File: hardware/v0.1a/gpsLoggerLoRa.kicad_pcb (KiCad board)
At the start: 4 copper layers, 40.9 x 72.7 mm, 108 parts, among them J1 USB_C_Receptacle, J3 DF12 - 10P, J4 CTX TAG Connect, P2 CONN_01X02, Q1 FG6943010R, SW1 SW_Push, U1 SKY13373, U2 MCP73832, U3 NCP167, U4 SKY13373, U5 MT25QL256ABA8E12, U6 NCP167, U8 ATSAMR34J18B, Y1 32.768kHz

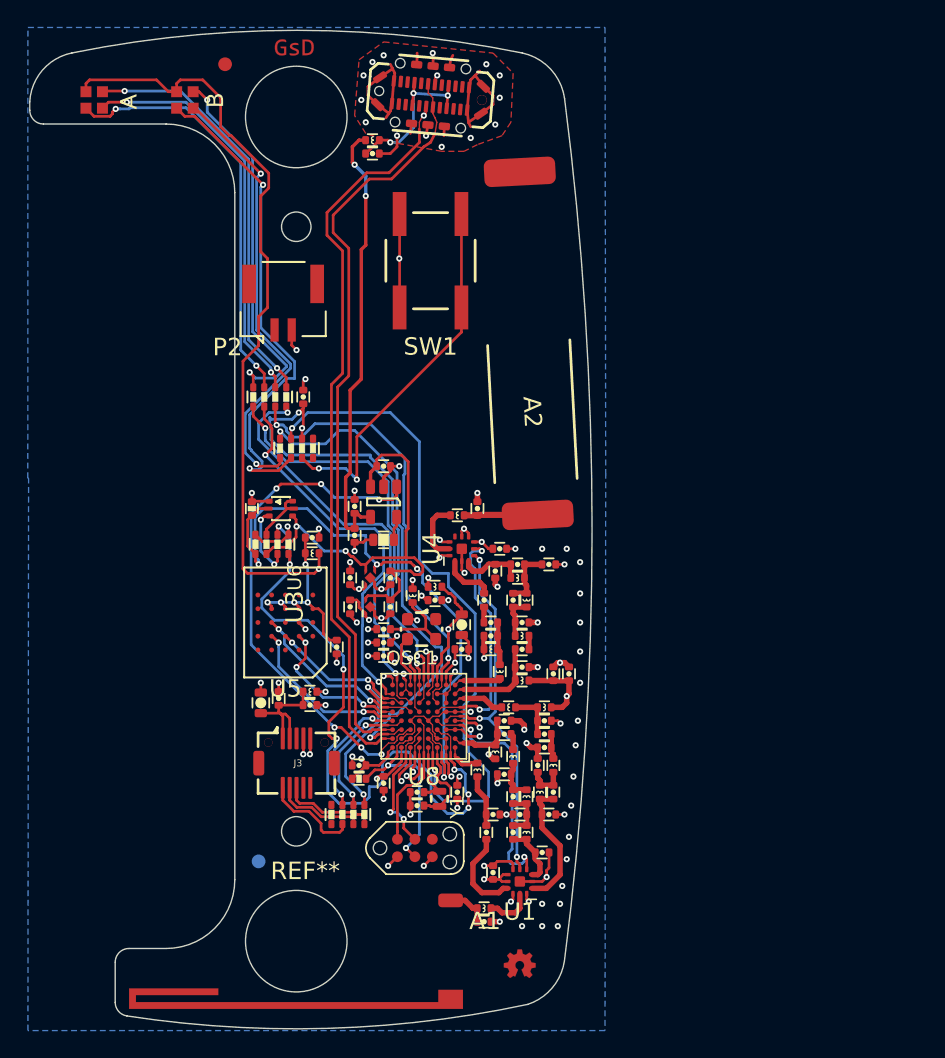
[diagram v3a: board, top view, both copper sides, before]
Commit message: Re-assigned IO pins. Added some extra filter as per Hardware guidelines.
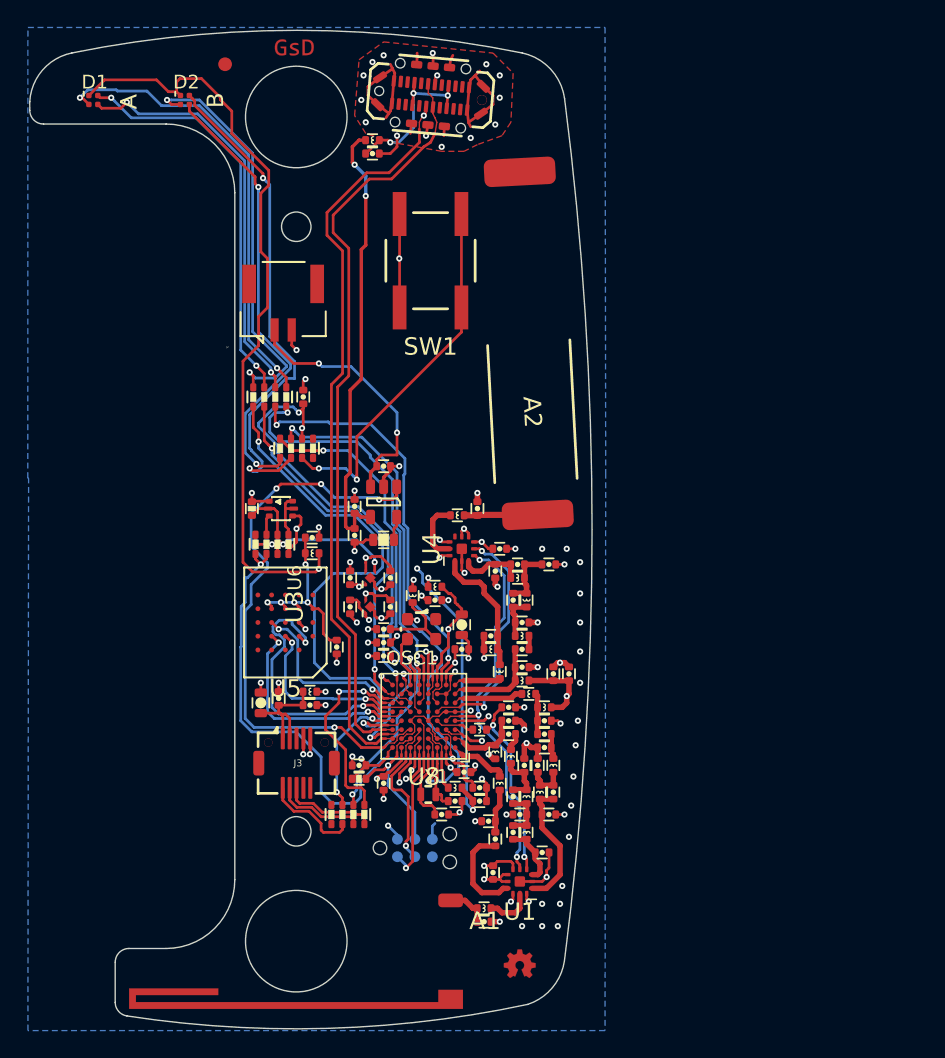
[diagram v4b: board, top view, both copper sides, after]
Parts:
- removed the REF** at (148.7, 126.7)
- added C57: 4.7pF, pkl_dipol:C_0402, F.Cu at (164.8, 121.3)
- added L23: 10nH, pkl_dipol:L_0402, F.Cu at (164.8, 117.1)
- added L24: 10nH, pkl_dipol:L_0402, F.Cu at (163.0, 121.3)
- C22, C27: value 18pF -> 4.7pF
- D1, D2: footprint footprints:LITEON_RGB -> gkl_led:0404LED_RGB
- J2: renamed from P2; value CONN_01X02 -> JST GH
- J4: moved to B.Cu
- moved C27 14.6 mm to (164.8, 122.3), turned to 180 degrees
- moved C22 6.31 mm to (166.9, 115.5)
- moved C50 2.78 mm to (163.0, 122.3), turned to 0 degrees
- moved C49 2.42 mm to (162.1, 123.3), turned to 180 degrees
- moved L11 1.90 mm to (166.3, 121.0)
- moved L2 1.76 mm to (168.4, 114.5)
- moved C20 1.60 mm to (168.1, 119.7), turned to 270 degrees
- moved C1 1.54 mm to (163.7, 120.2), turned to 0 degrees
- moved Y1 0.88 mm to (161.1, 121.8), turned to 0 degrees
- moved C34 0.81 mm to (166.0, 125.1)
- moved C13 0.59 mm to (165.5, 123.8), turned to 0 degrees
- moved C10 0.32 mm to (166.9, 117.4)
- moved C7 0.32 mm to (166.9, 116.5)
- moved L12 0.16 mm to (167.1, 119.0)
- moved D1 0.06 mm to (136.7, 71.3)
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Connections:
- C15 pad 1: Net-(C15-Pad1) -> /USB/VBAT
- C16 pad 1: Net-(C15-Pad1) -> /USB/VBAT
- C22 pad 1: Net-(C22-Pad1) -> GND
- C22 pad 2: Net-(C22-Pad2) -> /SAMR34/BAND_SEL
- C27 pad 1: Net-(C22-Pad2) -> GND
- C27 pad 2: Net-(C27-Pad2) -> /SAMR34/AUX_PWR_EN
- C5 pad 2: Net-(C22-Pad1) -> Net-(C5-Pad2)
- C52 pad 1: Net-(C15-Pad1) -> /USB/VBAT
- J2 pad 1: +BATT -> /USB/VBAT
- L1 pad 2: Net-(C22-Pad1) -> Net-(C5-Pad2)
- L18 pad 1: AVDD -> +3V3
- L18 pad 2: +3V3 -> AVDD
- L5 pad 2: Net-(C22-Pad1) -> Net-(C5-Pad2)
- Q1 pad 4: Net-(C15-Pad1) -> /USB/VBAT
- R6 pad 1: /SAMR34/AUX_PWR_EN -> /SAMR34/BATTERY_VOLTAGE
- R6 pad 3: Net-(C15-Pad1) -> /SAMR34/BATTERY_VOLTAGE
- R6 pad 4: Net-(Q1-Pad5) -> Net-(Q1-Pad3)
- R6 pad 5: Net-(Q1-Pad3) -> GND
- R6 pad 6: /SAMR34/BATTERY_VOLTAGE -> /SAMR34/AUX_PWR_EN
- R6 pad 7: /SAMR34/BATTERY_VOLTAGE -> /USB/VBAT
- R6 pad 8: GND -> Net-(Q1-Pad5)
- U2 pad 3: Net-(C15-Pad1) -> /USB/VBAT
- U3 pad 3: Net-(C15-Pad1) -> /USB/VBAT
- U3 pad 4: Net-(C15-Pad1) -> /USB/VBAT
- U4 pad 1: Net-(C27-Pad2) -> Net-(C5-Pad2)
- U6 pad 4: Net-(C15-Pad1) -> /USB/VBAT
- U8 pad C4: /SAMR34/AUX_PWR_EN -> Net-(L24-Pad2)
- U8 pad D3: /SAMR34/BAND_SEL -> Net-(L23-Pad2)
- U8 pad D7: /SAMR34/GPS_RX -> /SAMR34/LED_B_RED
- U8 pad E5: /SAMR34/LED_B_RED -> /SAMR34/GPS_RX
- U8 pad E6: /memio/DQ0 -> /SAMR34/FLASH_CS#
- U8 pad F5: /SAMR34/USER_BUTTON -> /SAMR34/LED_A_RED
- U8 pad F6: /SAMR34/LED_A_RED -> /SAMR34/USER_BUTTON
- U8 pad F7: /SAMR34/FLASH_CS# -> /memio/DQ0
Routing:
- net /USB/VBAT: track 0.00 -> 47.3 mm, vias 0 -> 5
- net Net-(C15-Pad1): track 35.6 -> 0.00 mm, vias 2 -> 0
- net AVDD: track 62.6 -> 45.5 mm
- net Net-(C5-Pad2): track 0.00 -> 9.56 mm
- net /SAMR34/FLASH_CLK: track 11.2 -> 20.5 mm, vias 3 -> 2
- net /SAMR34/LED_B_BLUE: track 49.1 -> 40.0 mm
- net /SAMR34/BATTERY_VOLTAGE: track 50.9 -> 41.7 mm, vias 7 -> 2
- net /SAMR34/LED_B_RED: track 31.1 -> 39.9 mm
- net /SAMR34/GPS_RX: track 9.78 -> 17.0 mm
- net /SAMR34/AUX_PWR_EN: track 45.4 -> 38.8 mm
- net Net-(L24-Pad2): track 0.00 -> 4.98 mm
- net /SAMR34/LED_B_GREEN: track 37.0 -> 32.1 mm
- net /USB/CHARGE_STAT: track 38.2 -> 42.4 mm, vias 6 -> 4
- net Net-(C27-Pad2): track 3.89 -> 0.00 mm
- net Net-(Q1-Pad3): track 5.24 -> 1.45 mm, vias 2 -> 0
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
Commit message: Small updates to the layout. Fixed up power planes. Passed DRC
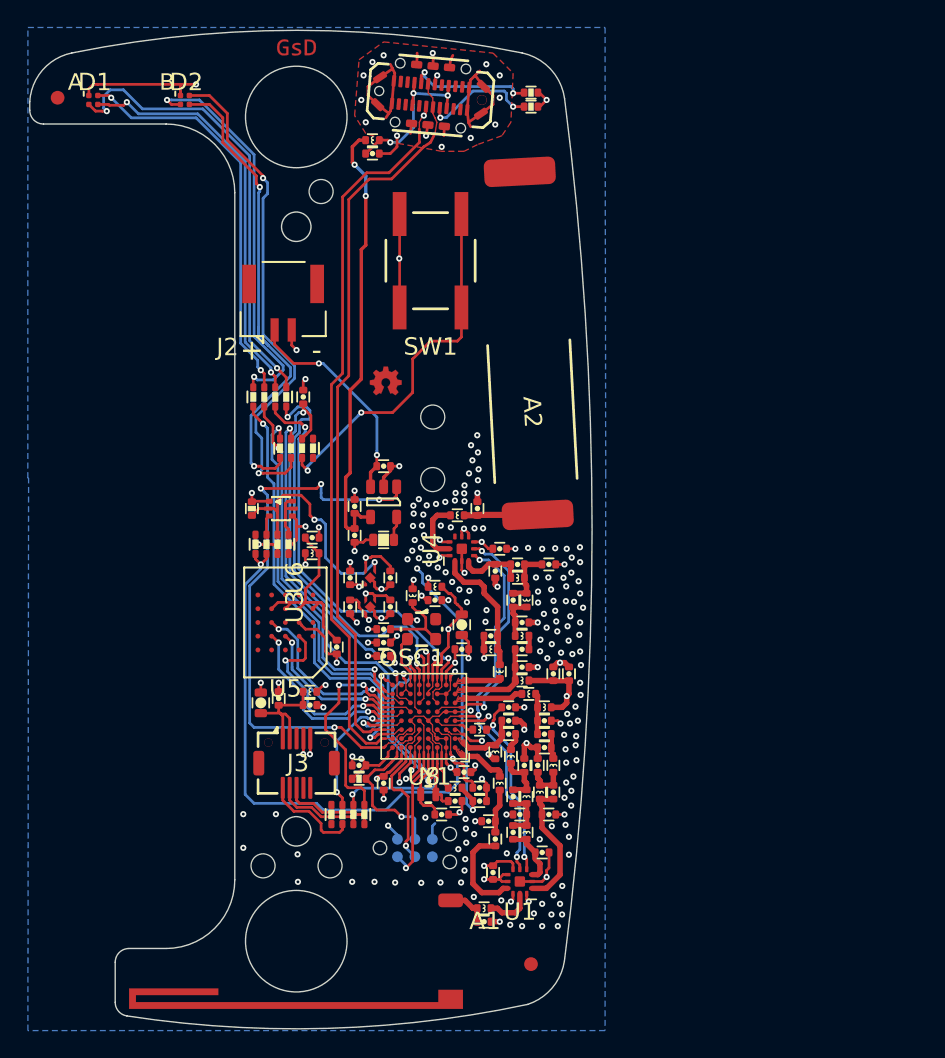
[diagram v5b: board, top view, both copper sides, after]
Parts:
- added R8: 5.1k, pkl_dipol:R_0402, F.Cu at (168.6, 71.8)
- added R9: 5.1k, pkl_dipol:R_0402, F.Cu at (168.6, 70.7)
- added REF**: Fiducial_1mm_Dia_2.54mm_Outer_CopperBottom, Fiducials:Fiducial_1mm_Dia_2.54mm_Outer_CopperBottom, B.Cu at (168.6, 134.2)
- added REF**: M1.6_Mounting Hole, M1.6_Mounting Hole, F.Cu at (153.3, 77.9)
- added REF**: M1.6_Mounting Hole, M1.6_Mounting Hole, F.Cu at (161.4, 94.3)
- added REF**: M1.6_Mounting Hole, M1.6_Mounting Hole, F.Cu at (161.4, 98.9)
- added REF**: M1.6_Mounting Hole, M1.6_Mounting Hole, F.Cu at (153.9, 127.0)
- added REF**: M1.6_Mounting Hole, M1.6_Mounting Hole, F.Cu at (149.1, 127.0)
- moved G*** 43.5 mm to (158.0, 91.8)
- moved REF** 12.4 mm to (134.1, 71.1)
- moved G*** 0.16 mm to (151.5, 67.5)
- turned L19 to 180 degrees
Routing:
- net Net-(J1-PadA5): track 0.00 -> 9.17 mm, vias 0 -> 2
- net Net-(J1-PadB5): track 0.00 -> 8.40 mm, vias 0 -> 2
- net /SAMR34/LED_B_RED: track 39.9 -> 32.7 mm
- net /SAMR34/FLASH_CLK: track 20.5 -> 14.3 mm
- net /USB/VBAT: track 47.3 -> 41.6 mm
- net /SAMR34/GPS_RX: track 17.0 -> 22.7 mm
- net GND: track 117.5 -> 122.7 mm, vias 92 -> 209
- net /SAMR34/LED_B_BLUE: track 40.0 -> 35.5 mm
- net /SAMR34/USER_BUTTON: track 33.5 -> 29.2 mm, vias 3 -> 2
- net /SAMR34/AUX_PWR_EN: track 38.8 -> 42.9 mm
- net /SAMR34/PP3V3_AUX: track 76.5 -> 73.1 mm, vias 4 -> 5
- net +3V3: track 44.3 -> 47.2 mm
- net Net-(D2-Pad3): track 33.2 -> 35.7 mm
- net /SAMR34/BATTERY_VOLTAGE: track 41.7 -> 44.1 mm
- net /memio/DQ1: track 16.5 -> 14.2 mm
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- added copper zone on F.Cu, net /SAMR34/PA_BOOST
- added copper zone on F.Cu, net /SAMR34/RFI_HF
- added copper zone on F.Cu, net /SAMR34/RFI_LF
- added copper zone on F.Cu, net /SAMR34/RFO_HF
- added copper zone on F.Cu, net /SAMR34/RFO_LF
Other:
- board text added: "+"
- board text added: "-"

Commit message: Added Vcore Cap. Missing from Microchips app note reference schematic
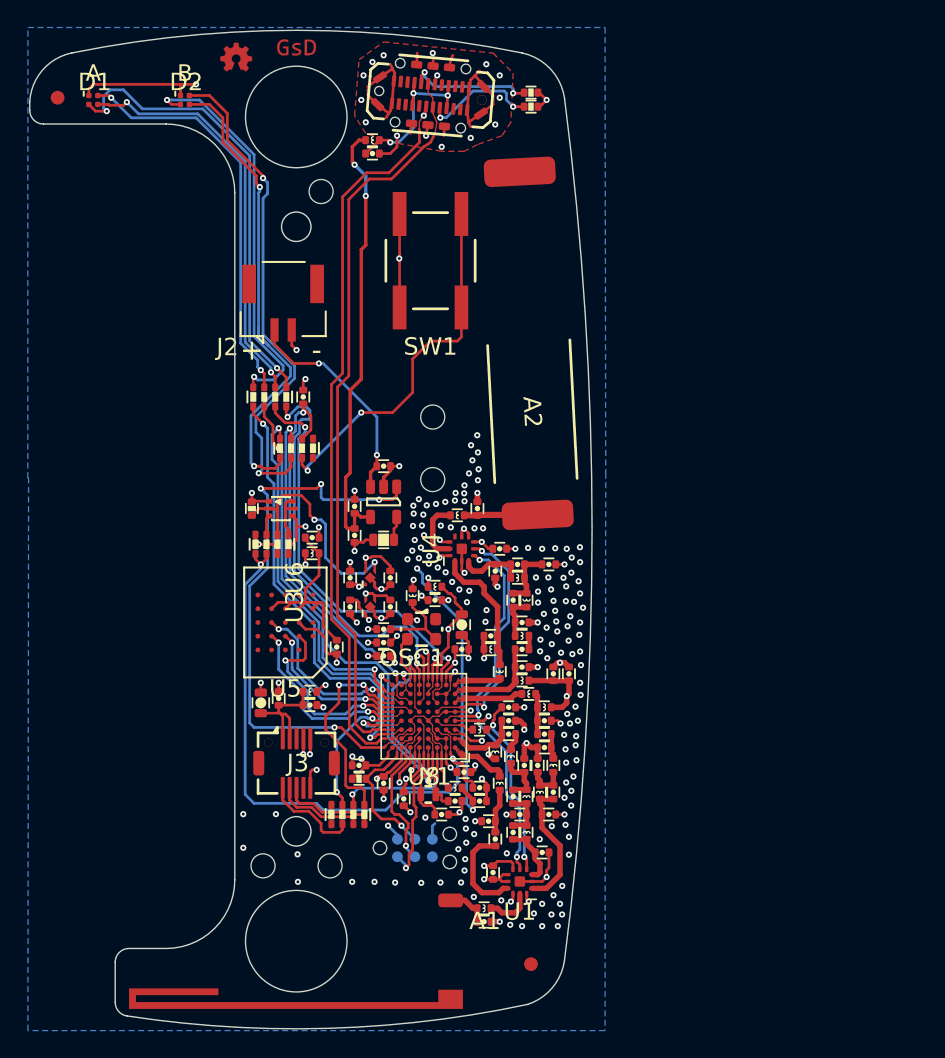
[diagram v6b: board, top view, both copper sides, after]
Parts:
- added C58: 1uF, pkl_dipol:C_0402, F.Cu at (159.3, 122.1)
- C43: value 100nF -> 1uF
- moved G*** 26.0 mm to (147.1, 68.2)
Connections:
- J3 pad 10: Net-(J3-Pad10) -> +3V3
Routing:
- net +3V3: track 47.2 -> 52.5 mm, vias 8 -> 9
- net Net-(C58-Pad2): track 3.86 -> 4.89 mm
- net GND: track 122.7 -> 123.4 mm, vias 209 -> 210
- net /SAMR34/RESET: track 12.0 -> 11.4 mm

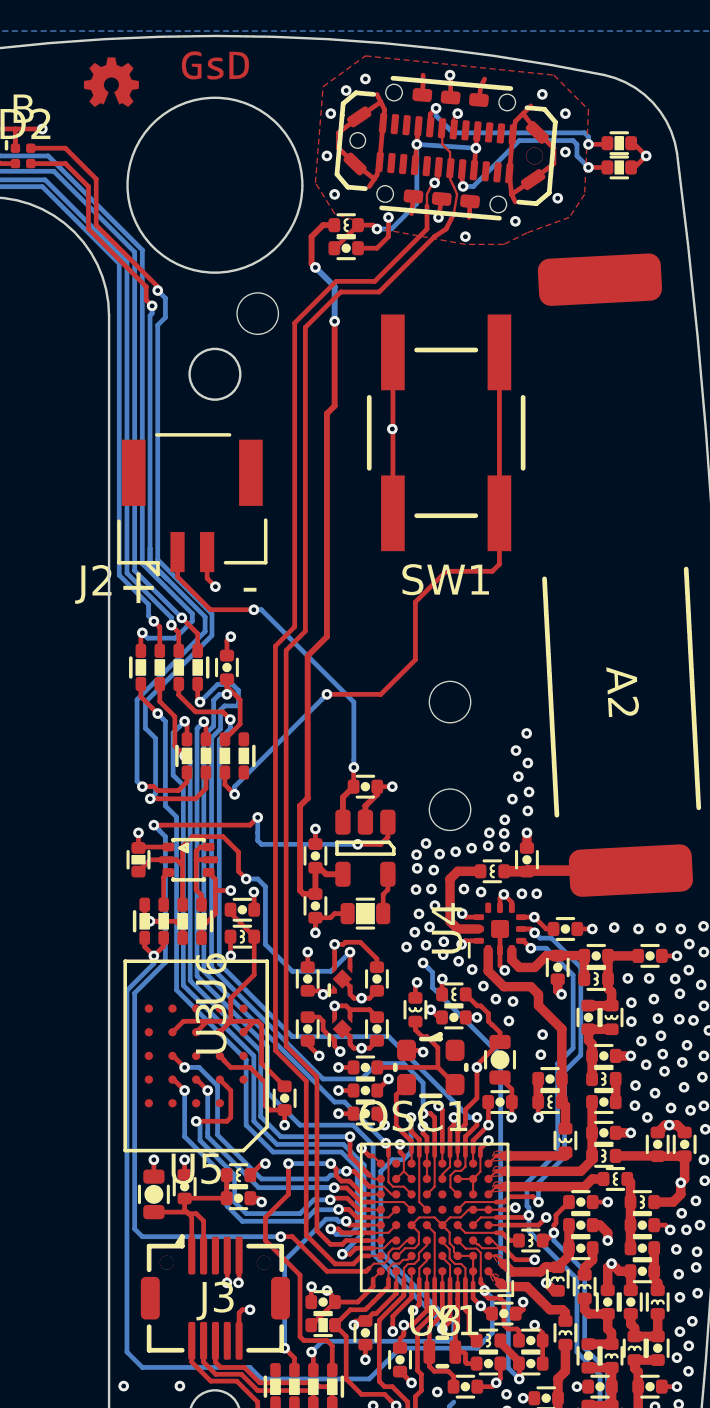
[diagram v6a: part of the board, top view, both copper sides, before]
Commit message: Added TVS diode to USB input.
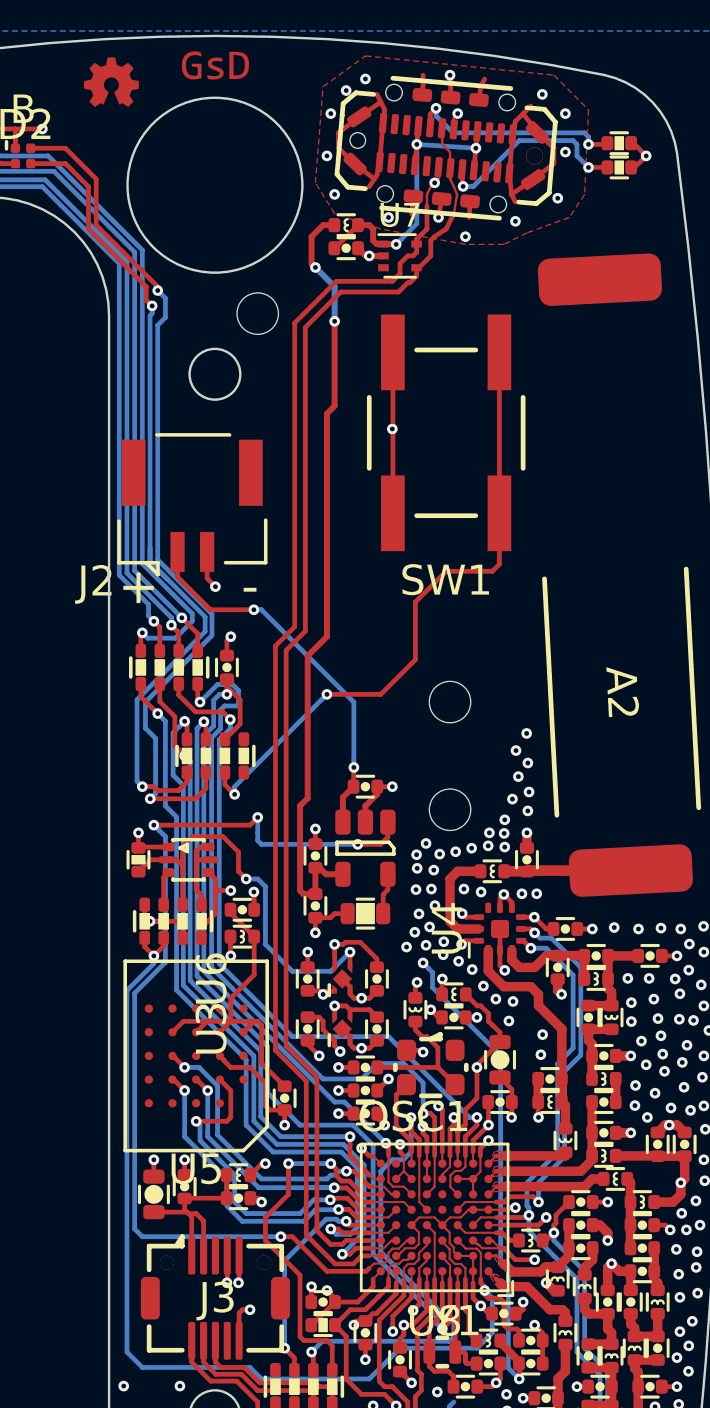
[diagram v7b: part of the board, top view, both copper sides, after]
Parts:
- added U7: NUP2114, Package_TO_SOT_SMD:SOT-553, F.Cu at (159.3, 75.5)
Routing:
- net Net-(C9-Pad1): track 12.7 -> 14.0 mm
- net /SAMR34/USB_DATA_P: track 54.2 -> 54.8 mm
- net /SAMR34/USB_DATA_N: track 57.0 -> 57.6 mm
- net GND: track 123.4 -> 122.9 mm, vias 210 -> 211

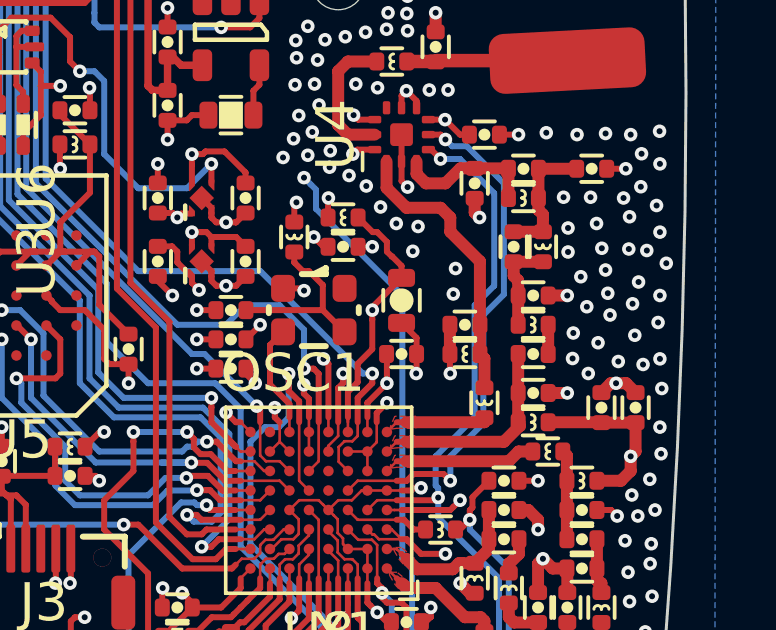
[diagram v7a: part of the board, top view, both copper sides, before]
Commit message: Checked RF filters with reference schematics. Updated all Part Numbers for BOM.
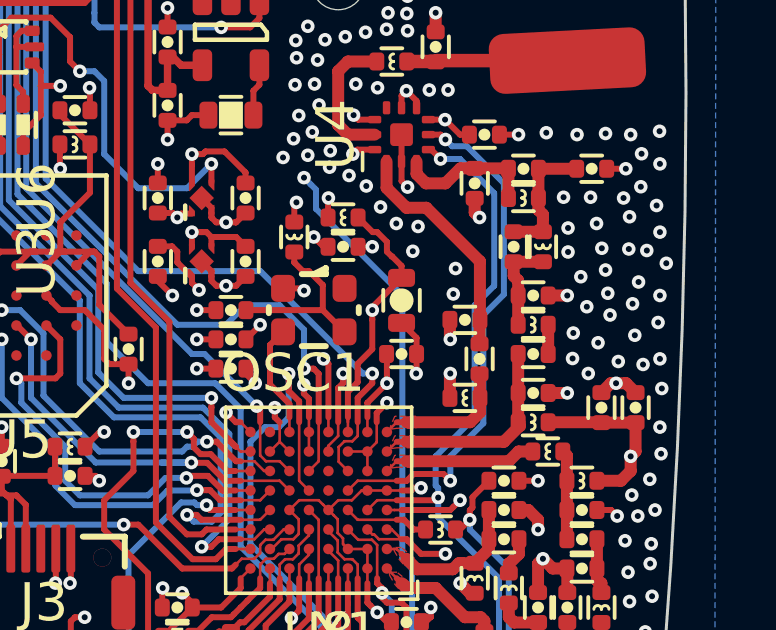
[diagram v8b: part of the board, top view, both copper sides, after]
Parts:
- removed L5: 33nH, pkl_dipol:L_0402
- added C59: 4.7pF, pkl_dipol:C_0402, F.Cu at (166.1, 111.4)
- C19: value 22pF -> 0R
- C24: value 8.2pF -> 6.8pF
- C25: value DNP -> 2.7pF
- C26: value 5.6pF -> 6.8pF
- C29: value 3.3pF -> DNP
- C4: value 3.9pF -> 4.7pF
- C5: value 3.9pF -> DNP
- L1: value 2.2nH -> 18nH
- L6: value 33nH -> 82nH
- L7: value 11nH -> 15nH
- L8: value 10nH -> 12nH
- L9: value 10nH -> 0R
- moved L1 0.67 mm to (165.6, 112.7), turned to 0 degrees
- moved C5 0.16 mm to (165.6, 110.1)
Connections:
- L1 pad 1: /SAMR34/RFI_LF -> GND
- L1 pad 2: Net-(C5-Pad2) -> /SAMR34/RFI_LF
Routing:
- net Net-(C5-Pad2): track 9.56 -> 7.76 mm
- net /SAMR34/RFI_LF: track 3.48 -> 4.66 mm
- net GND: track 122.9 -> 122.8 mm, vias 211 -> 212
